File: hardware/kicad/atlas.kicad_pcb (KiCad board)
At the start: 4 copper layers, 38.4 x 82.2 mm, 118 parts, among them J1 U262-161N-4BVC11, J2 +LIPO, J3 -LIPO, J4 HC-FPC-05-09-24RLTAG, Q1 DMG1012UW, Q4 PMV32UP, Q5 DMG1012UW, Q6 AO3407A, Q7 SI1308EDL, Q8 PMV32UP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

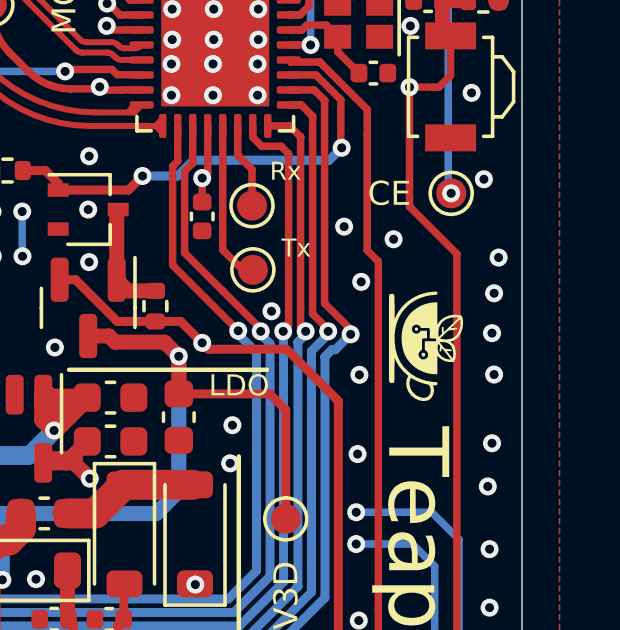
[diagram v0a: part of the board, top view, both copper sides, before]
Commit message: Added a button for menu control (only pcb and no routing)
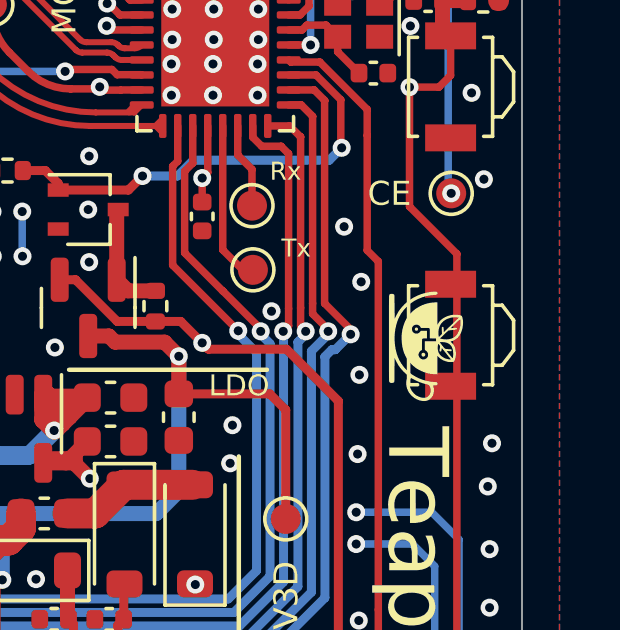
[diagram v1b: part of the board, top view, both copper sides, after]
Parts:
- added SW1: B3U-3000P, atlas:SW_SPST_B3U-3000P, F.Cu at (126.5, 54.0)
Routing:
- net GND: vias 280 -> 275

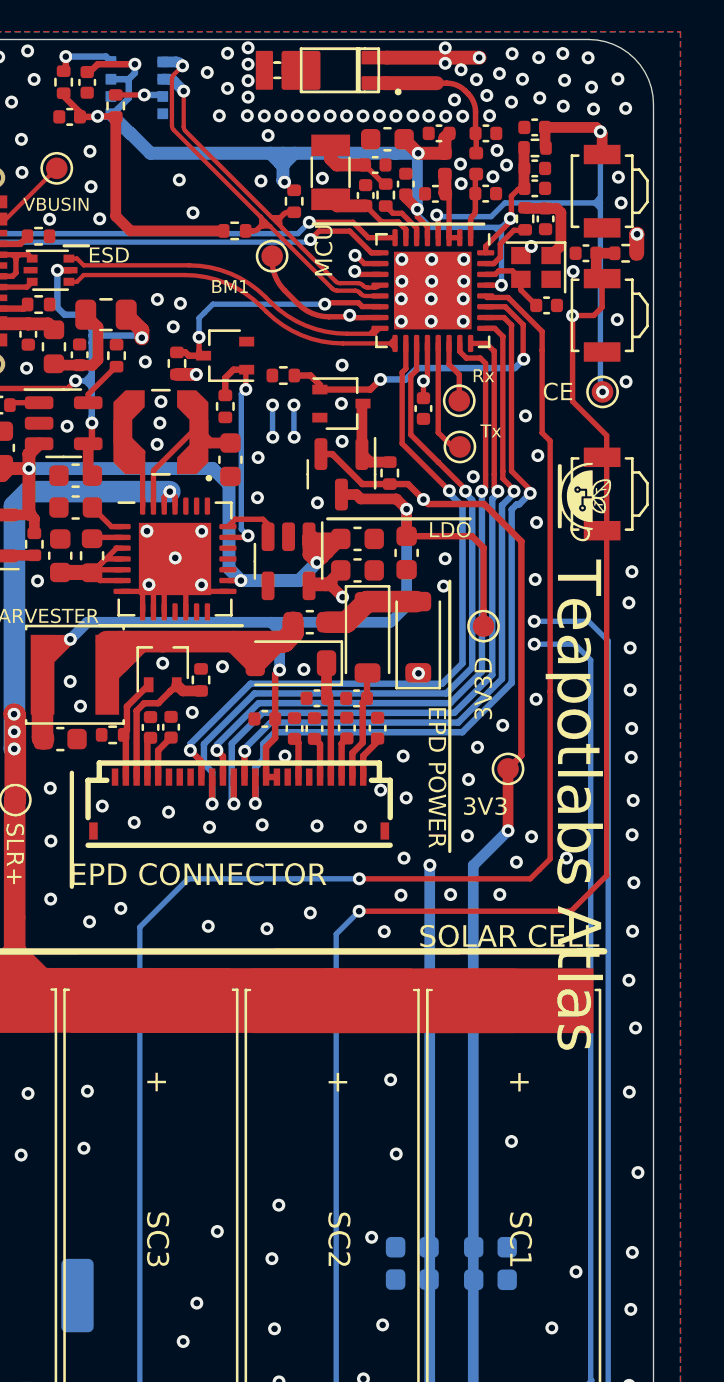
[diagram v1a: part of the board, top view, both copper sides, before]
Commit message: add second user button
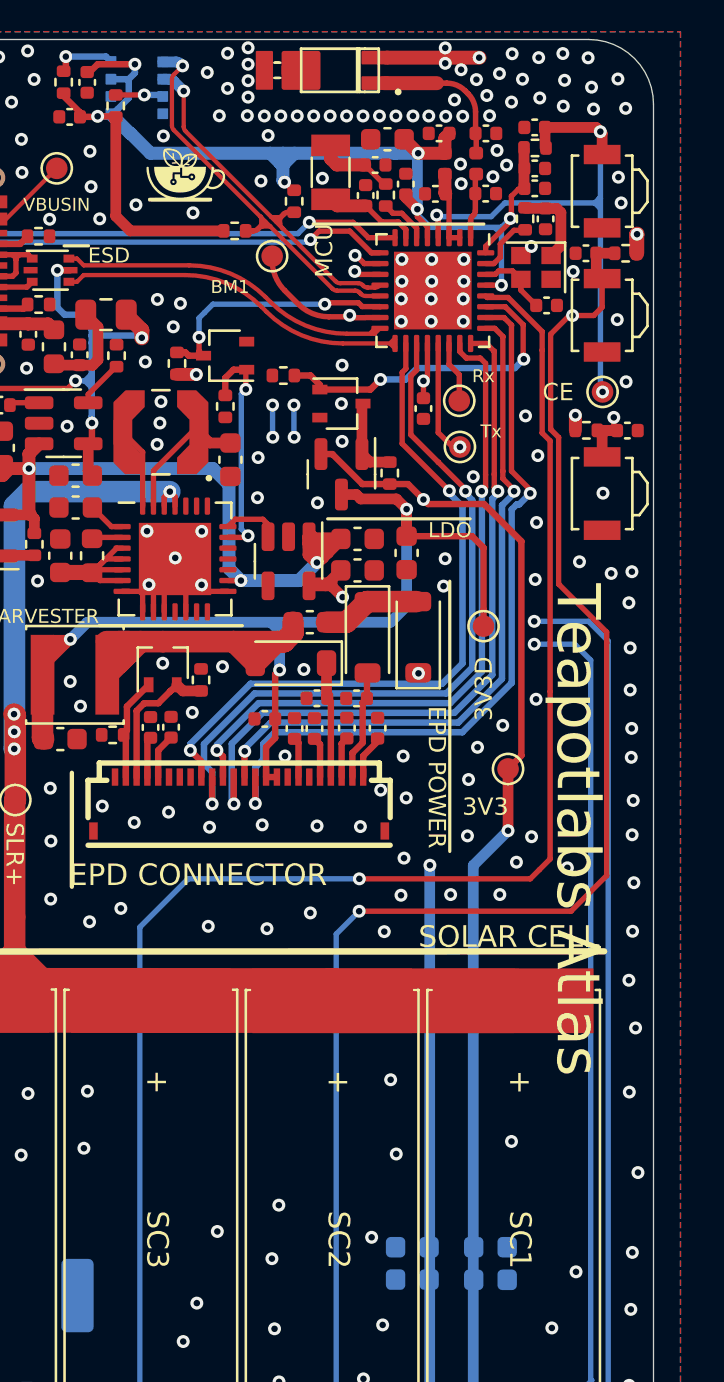
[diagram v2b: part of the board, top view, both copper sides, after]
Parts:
- removed the SW1 at (126.5, 54.0)
- added C30: 100n, Capacitor_SMD:C_0402_1005Metric, F.Cu at (127.7, 51.1)
- added R5: 5K1, Resistor_SMD:R_0402_1005Metric, F.Cu at (125.8, 51.0)
- added SW3: B3U-3000P, atlas:SW_SPST_B3U-3000P, F.Cu at (126.5, 54.0)
- moved G*** 23.9 mm to (107.2, 39.2), turned to 0 degrees
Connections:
- net Net-(U1-U0RXD/GPIO17/FSPICS1) renamed /Main Controller/USER_BTN1
- net Net-(U1-U0TXD/GPIO16/FSPICS0) renamed /Main Controller/USER_BTN0
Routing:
- net /Main Controller/USER_BTN0: track 5.41 -> 16.0 mm, vias 0 -> 2
- net +3V3: track 179.0 -> 185.2 mm, vias 13 -> 14
- net /Main Controller/BOOT_MODE1: track 95.8 -> 96.7 mm
- net GND: vias 275 -> 279

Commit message: added led symbols and placements on pcb.
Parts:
- added LED**: LTSTS220KGKT, ltst-220:LTSTS220KGKT, B.Cu at (85.6, 37.5)
- added LED**: LTSTS220KGKT, ltst-220:LTSTS220KGKT, B.Cu at (130.0, 48.9)
- added LED**: LTSTS220KGKT, ltst-220:LTSTS220KGKT, B.Cu at (131.0, 76.1)
- added LED**: LTSTS220KGKT, ltst-220:LTSTS220KGKT, B.Cu at (131.8, 96.2)
- added LED**: LTSTS220KGKT, ltst-220:LTSTS220KGKT, B.Cu at (87.3, 78.5)
- added LED**: LTSTS220KGKT, ltst-220:LTSTS220KGKT, B.Cu at (131.5, 106.5)
- added LED**: LTSTS220KGKT, ltst-220:LTSTS220KGKT, B.Cu at (130.9, 40.0)
- added LED**: LTSTS220KGKT, ltst-220:LTSTS220KGKT, B.Cu at (87.1, 95.1)
- added LED**: LTSTS220KGKT, ltst-220:LTSTS220KGKT, B.Cu at (86.9, 69.0)
- added LED**: LTSTS220KGKT, ltst-220:LTSTS220KGKT, B.Cu at (131.1, 57.6)
- added LED**: LTSTS220KGKT, ltst-220:LTSTS220KGKT, B.Cu at (86.2, 58.4)
- added LED**: LTSTS220KGKT, ltst-220:LTSTS220KGKT, B.Cu at (87.0, 86.8)
- added LED**: LTSTS220KGKT, ltst-220:LTSTS220KGKT, B.Cu at (85.4, 48.4)
- added LED**: LTSTS220KGKT, ltst-220:LTSTS220KGKT, B.Cu at (129.8, 65.5)
- added LED**: LTSTS220KGKT, ltst-220:LTSTS220KGKT, B.Cu at (130.9, 85.7)

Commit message: Revert "added led symbols and placements on pcb."
This reverts commit 775bc6ae91366f689438663b29cde4e2220ca0a7.
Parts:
- removed LED** (x15): LTSTS220KGKT, ltst-220:LTSTS220KGKT
